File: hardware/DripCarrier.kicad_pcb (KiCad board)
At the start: 2 copper layers, 150 x 110 mm, 47 parts, among them J1 12V IN, J10 FLOW, J11 RAIN SW, J12 LDR, J3 12V VALVES, J4 12V PUMP, J5 RELAY 2: +5 GND FILL DRAIN, J6 RELAY 8: +5 GND IN1..IN8, J7 RELAY 1: +5 GND PUMP, J8 SD D1 mini, J9 DS3231, SW1 RESET CFG, U1 ESP32 DevKitC 38, U2 DC-DC 12-5V 2A, U3 DC-DC 5-3.3V, U4 PCF8574P, U5 74HC4051, U6 LIGHT LM393

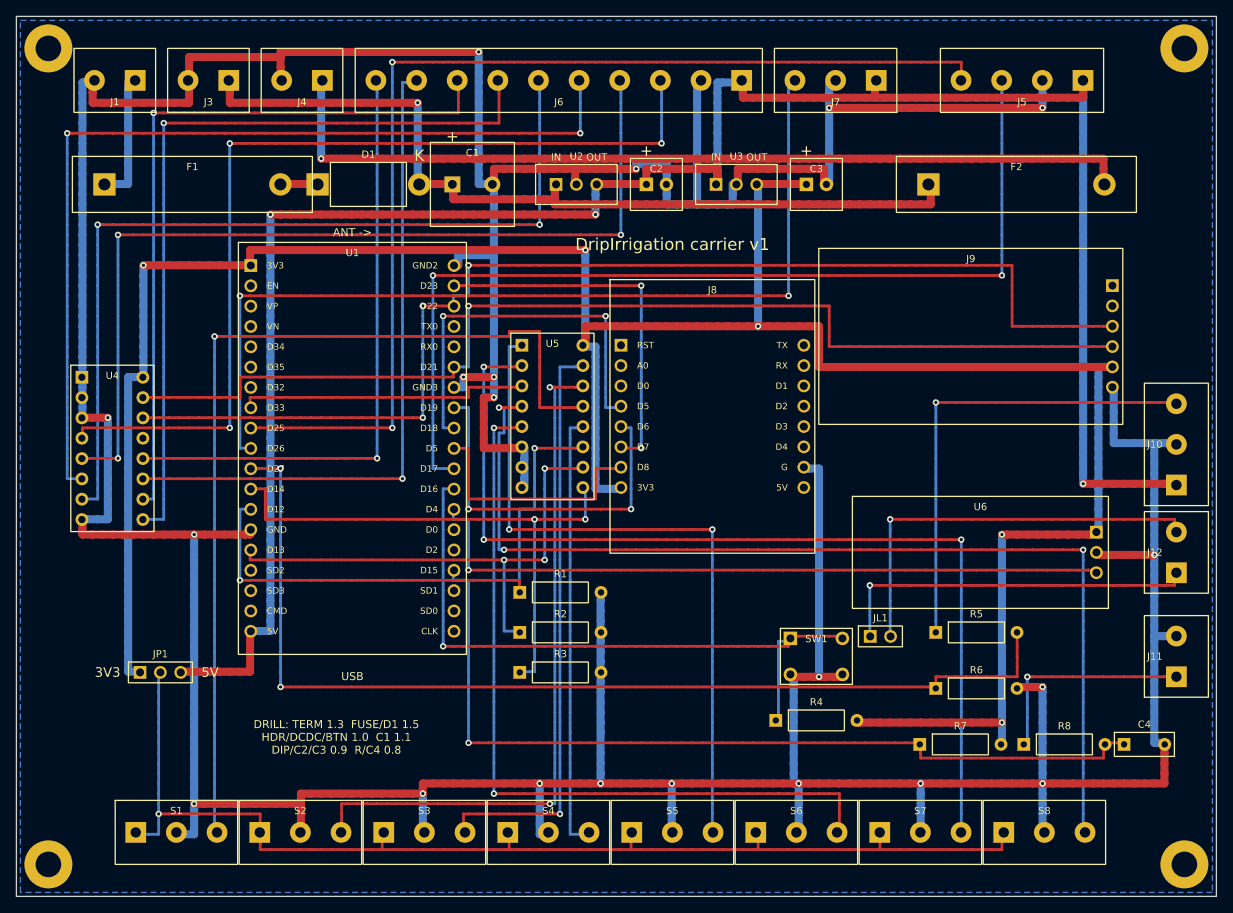
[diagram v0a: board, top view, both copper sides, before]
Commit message: fix(hardware): ревизия платы, скриптов и документации
Схема:
- кнопка сброса: R4 теперь тянет GPIO16 к земле, кнопка замыкает на 3,3 В (как ждёт прошивка)
- защита от переполюсовки: P-MOSFET IRF4905 (Q1, R9) вместо диода 1N5822 — без нагрева при 5 А
- TVS P6KE18CA (D2) на шине 12 В, развязка C5/C6, подтяжки I2C R10/R11
- делитель расходомера R6 20k→33k (учтена внутренняя подтяжка YF-S201)
- 3V3 модуля ESP32 отвязан от шины 3,3 В (два стабилизатора на одной шине)
- ширина дорожек по цепям: 12 В — 2 мм, 5 В — 1,2 мм

Генератор: детерминированные UUID, учёт зоны под винты М3, запрет двух
переходов подряд, исправлены подписи выводов в SVG, удалён мёртвый код.
Скрипты: DRC возвращает ошибку при нарушениях, render_steps без cygpath,
просмотрщик подсвечивает все части модуля и не ловит скрытые.
Документы: обновлены схема, BOM, сборка, README ссылается на плату.

Co-Authored-By: Claude Fable 5.1 <noreply@anthropic.com>
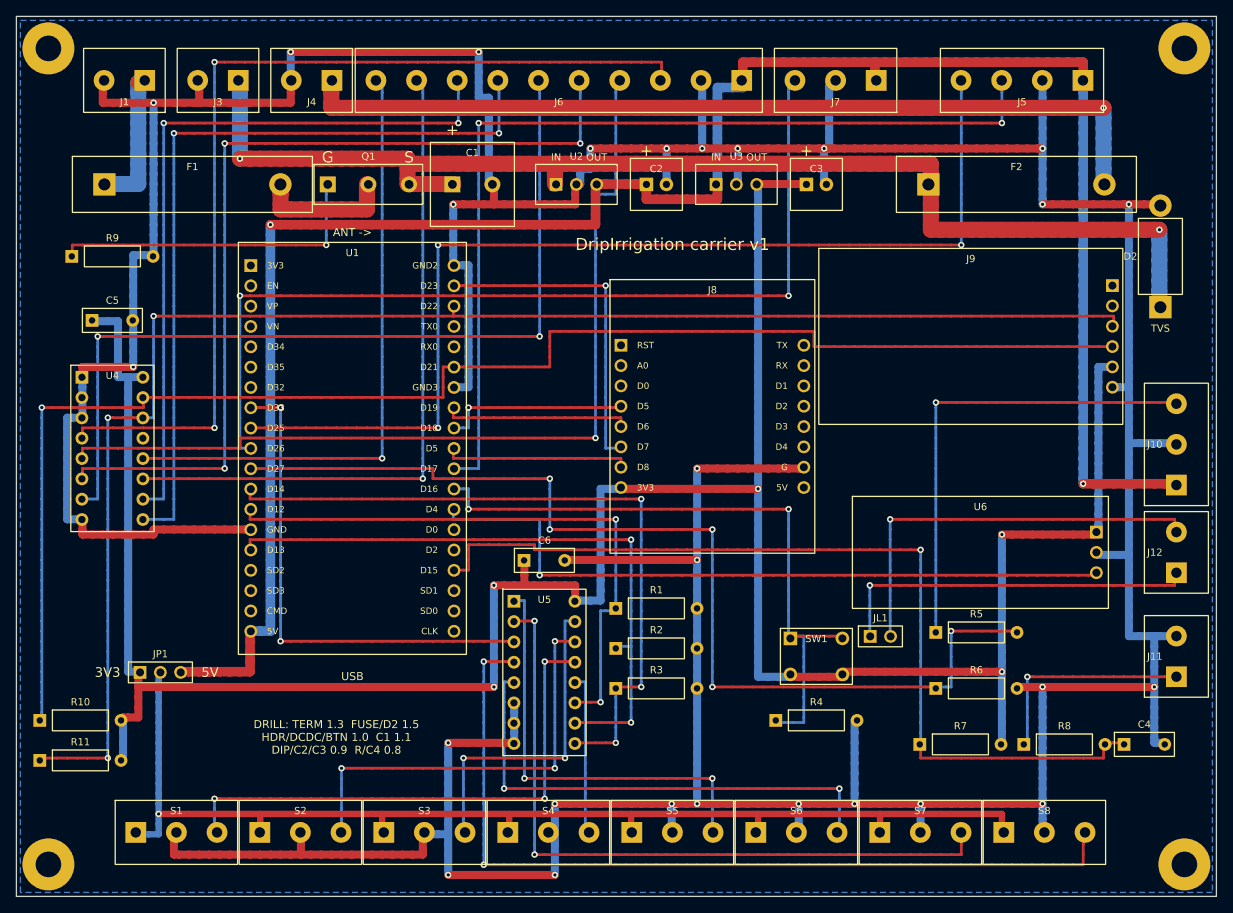
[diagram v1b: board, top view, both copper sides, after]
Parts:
- removed D1: 1N5822, DripCarrier:DO201
- added C5: 100n, DripCarrier:CAP_C5, F.Cu at (12.0, 38.0)
- added C6: 100n, DripCarrier:CAP_C5, F.Cu at (66.0, 68.0)
- added D2: P6KE18CA, DripCarrier:DO201, F.Cu at (143.0, 30.0)
- added Q1: IRF4905, DripCarrier:TO220_2, F.Cu at (44.0, 21.0)
- added R10: 4.7k, DripCarrier:R_AX, F.Cu at (8.00, 88.0)
- added R11: 4.7k, DripCarrier:R_AX, F.Cu at (8.00, 93.0)
- added R9: 10k, DripCarrier:R_AX, F.Cu at (12.0, 30.0)
- R6: value 20k -> 33k
- moved U5 32.0 mm to (66.0, 82.0)
- moved R1 12.2 mm to (80.0, 74.0)
- moved R2 12.2 mm to (80.0, 79.0)
- moved R3 12.2 mm to (80.0, 84.0)
- moved J1 1.20 mm to (13.5, 8.00)
- moved J3 1.20 mm to (25.2, 8.00)
- moved J4 1.20 mm to (36.9, 8.00)
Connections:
- R4 pad 2: +3V3 -> GND
- SW1 pad 3: GND -> +3V3
- SW1 pad 4: GND -> +3V3
- U1 pad 3V3: +3V3 -> (no net)
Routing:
- net Y0: track 118.7 -> 66.7 mm, vias 1 -> 3
- net SDA: track 137.8 -> 184.8 mm
- net +12V: track 107.3 -> 153.7 mm, vias 1 -> 2
- net SCL: track 148.0 -> 191.8 mm
- net QG: track 0.00 -> 40.6 mm, vias 0 -> 1
- net Y5: track 97.8 -> 62.2 mm
- net Y6: track 123.2 -> 87.6 mm, vias 3 -> 2
- net Y1: track 87.6 -> 53.3 mm, vias 2 -> 3
- net Y4: track 88.3 -> 54.0 mm
- net Y3: track 55.2 -> 21.0 mm
- net Y2: track 73.7 -> 40.6 mm, vias 1 -> 2
- net SD_SCK: track 48.9 -> 23.5 mm, vias 2 -> 1
- net ADC: track 36.8 -> 62.2 mm, vias 0 -> 2
- net Y7: track 130.8 -> 107.9 mm, vias 3 -> 2
- net SD_MISO: track 46.4 -> 23.5 mm, vias 2 -> 0
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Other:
- board text added: "DRILL: TERM 1.3 FUSE/D2 1.5"
- board text added: "G"
- board text added: "S"
- board text added: "TVS"
- board text removed: "DRILL: TERM 1.3 FUSE/D1 1.5"
- board text removed: "K"

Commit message: fix(hardware): подписи полярности клемм, квадратные площадки в SVG, концы дорожек в центрах площадок
Co-Authored-By: Claude Fable 5.1 <noreply@anthropic.com>
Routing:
- net SENS_V: track 146.7 -> 144.8 mm
- net +5V: track 259.7 -> 258.5 mm
- net GND: track 706.1 -> 707.3 mm
- net Y3: track 21.0 -> 20.2 mm
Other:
- board text added: "+12"
- board text added: "+5"
- board text added: "GND"

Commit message: feat(hardware): подписи выводов гнёзд J9, U6 и штырей JL1 на шелкографии
Co-Authored-By: Claude Opus 5 <noreply@anthropic.com>
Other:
- board text added: "32K"
- board text added: "DO"
- board text added: "LDR1"
- board text added: "LDR2"
- board text added: "SCL"
- board text added: "SDA"
- board text added: "SQW"
- board text added: "VCC"
